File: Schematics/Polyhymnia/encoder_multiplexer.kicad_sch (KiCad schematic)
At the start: 10 parts, among them SW1 Filter Cutoff, SW2 Filter Resonance, SW3 OSC1 Type, SW4 OSC1 Detune, SW5 Filter Resonance, SW6 OSC2 Type, SW7 OSC2 Detune, SW8 OSC3 Type, SW9 OSC3 Detune, U6 ATmega32-16P

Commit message: Cleaned up wiring
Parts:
- removed SW5: Filter Resonance, symbol Device:RotaryEncoder
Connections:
- net 3.3V: now also U6.30 (AVCC)
- net at SW2.A: now also U6.38 (PA2)
- net at SW2.B: now also U6.37 (PA3)
- net at U6.39 (PA1): now also SW1.B
- net at U6.40 (PA0): now also SW1.A

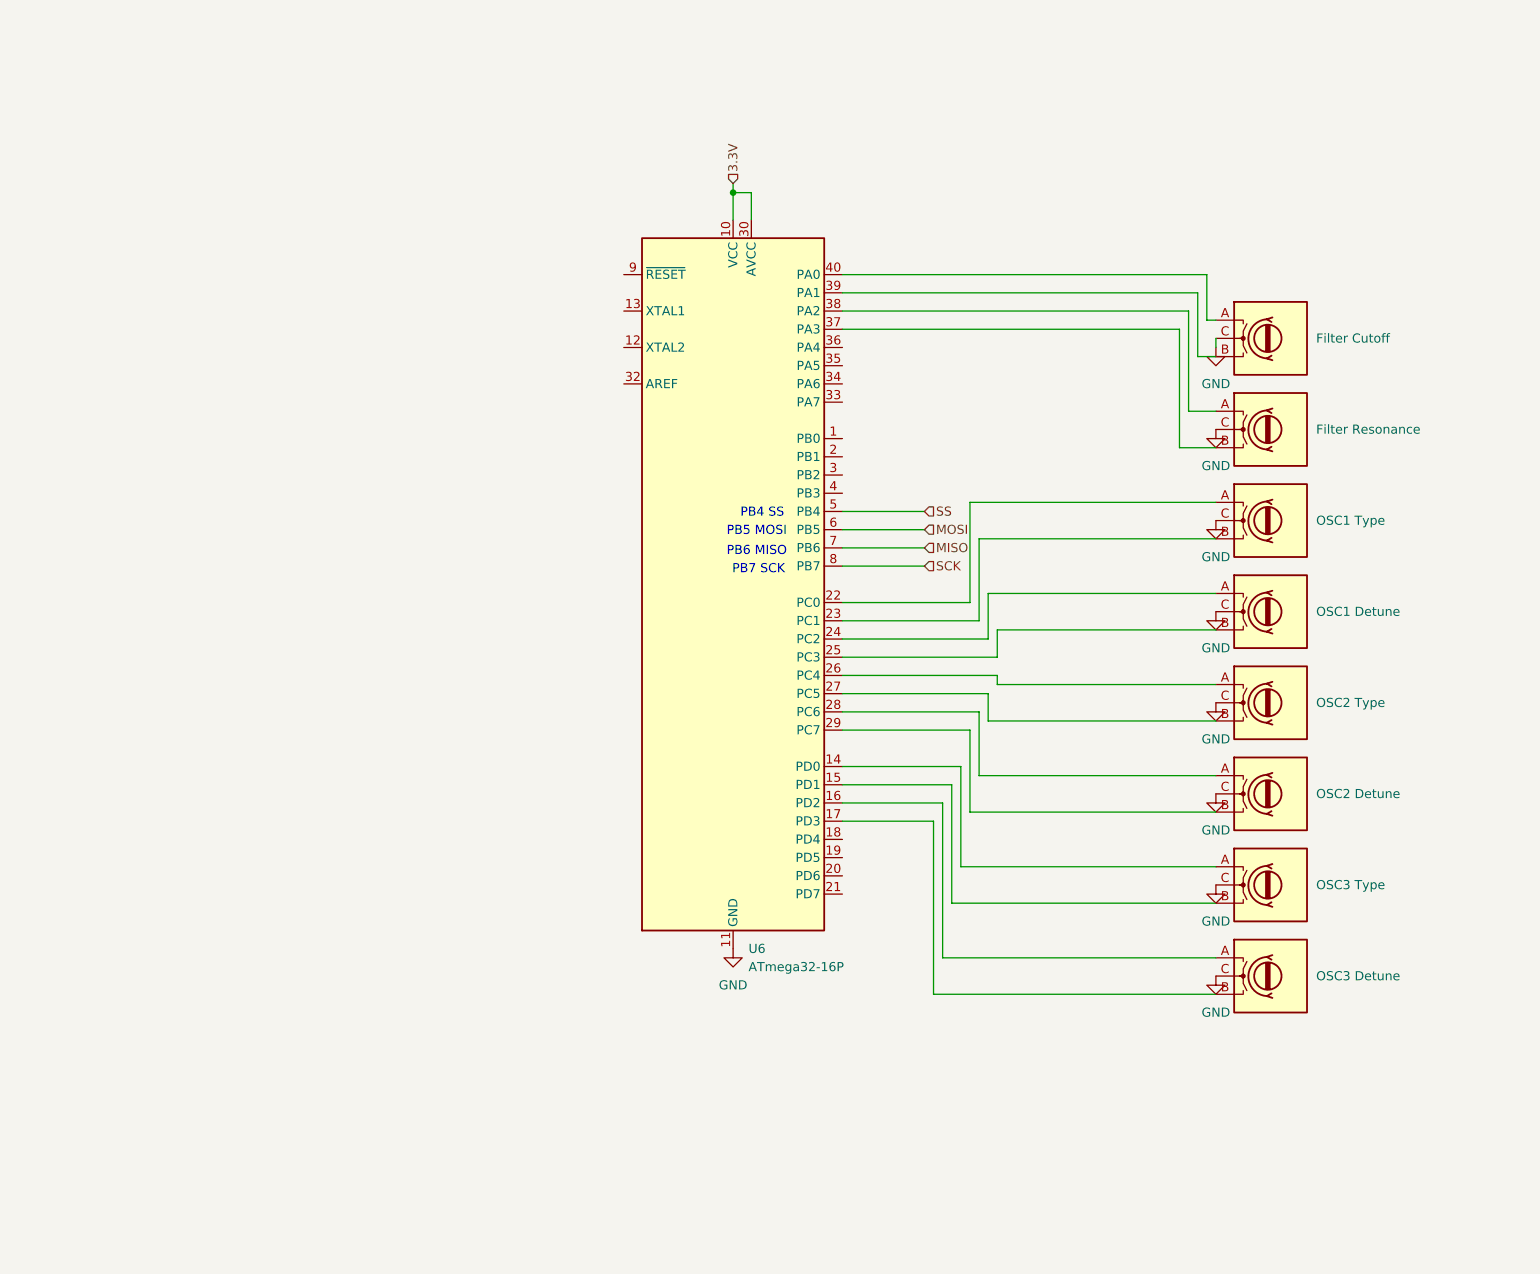
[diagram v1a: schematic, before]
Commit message: Added schematics for OSC, Filter and Envelope and updated README
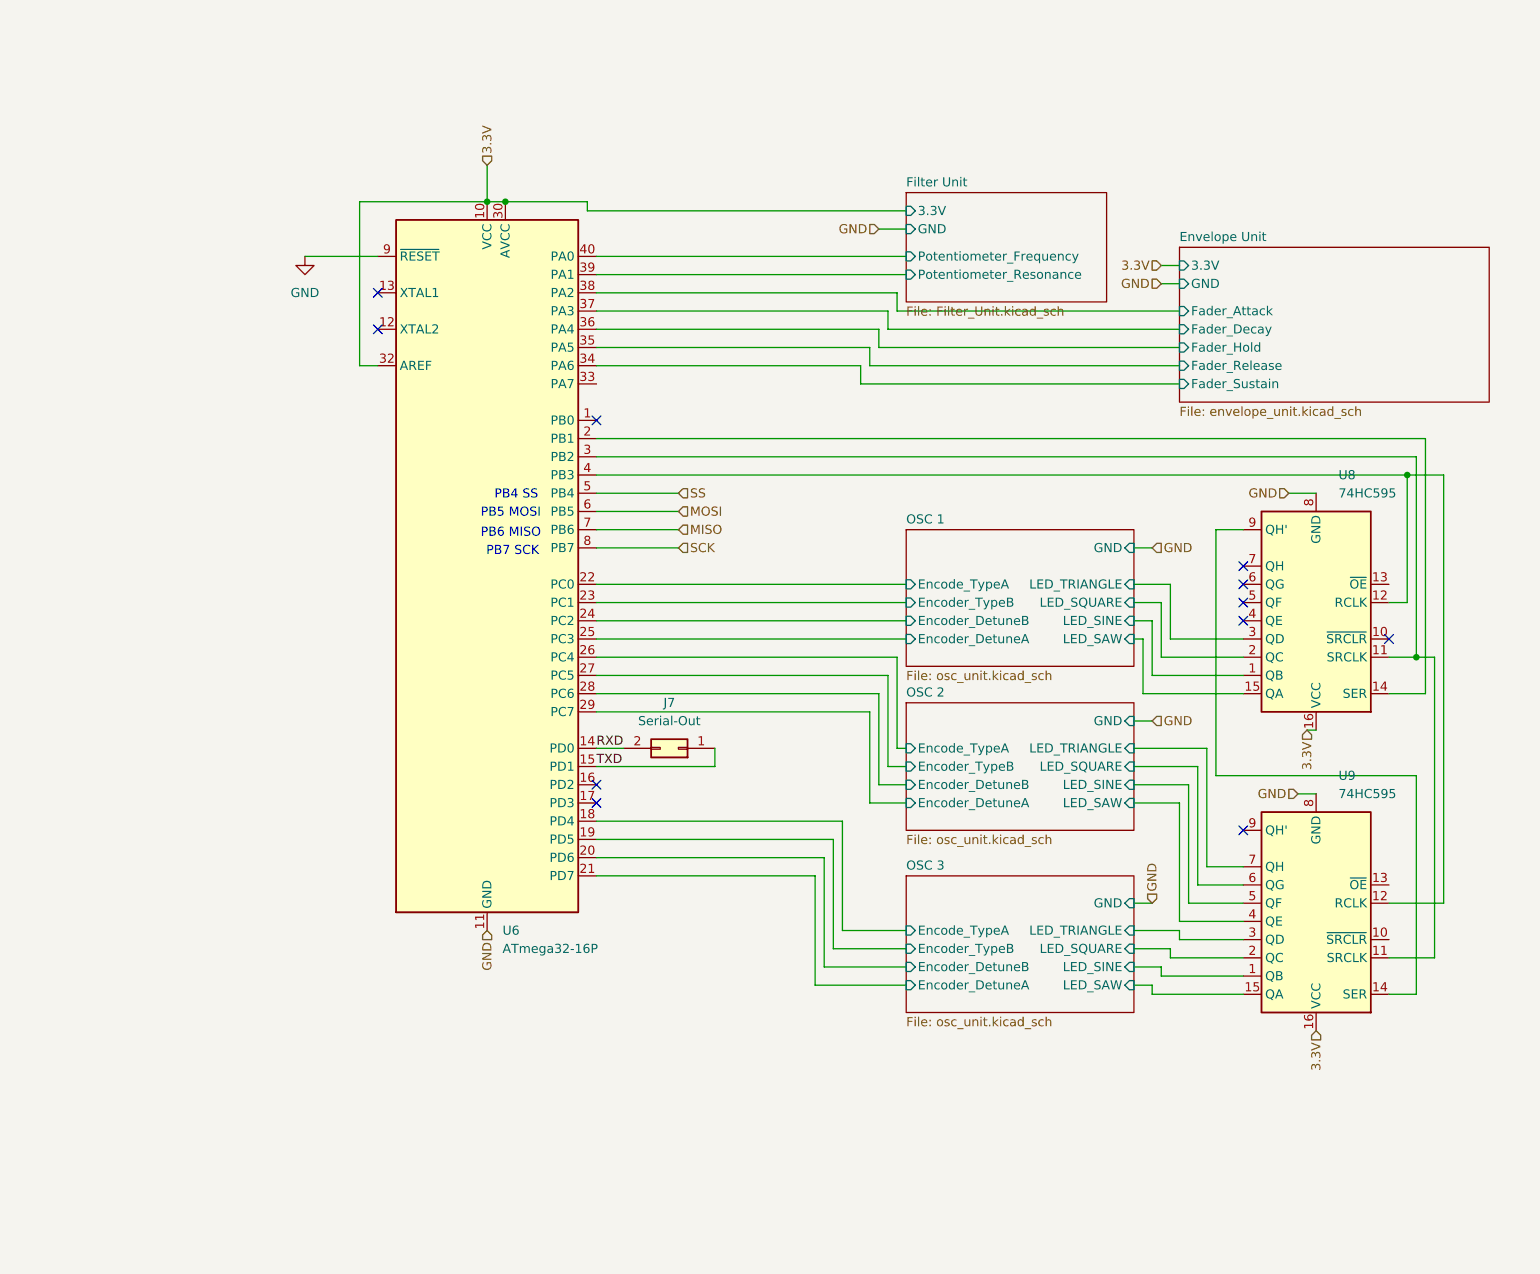
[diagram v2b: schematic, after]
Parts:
- removed SW1: Filter Cutoff, symbol Device:RotaryEncoder
- removed SW2: Filter Resonance, symbol Device:RotaryEncoder
- removed SW3: OSC1 Type, symbol Device:RotaryEncoder
- removed SW4: OSC1 Detune, symbol Device:RotaryEncoder
- removed SW6: OSC2 Type, symbol Device:RotaryEncoder
- removed SW7: OSC2 Detune, symbol Device:RotaryEncoder
- removed SW8: OSC3 Type, symbol Device:RotaryEncoder
- removed SW9: OSC3 Detune, symbol Device:RotaryEncoder
- added J7: Serial-Out, symbol Connector_Generic:Conn_02x01
- added U8, U9: 74HC595, symbol 74xx:74HC595
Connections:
- net 3.3V: now also U6.32 (AREF), U8.16 (VCC), U9.16 (VCC)
- net GND: now also U6.9 (~{RESET}), U8.8 (GND), U9.8 (GND)
- net Envelope Unit/Fader_Attack: now reaches U6.38 (PA2)
- net Envelope Unit/Fader_Decay: now reaches U6.37 (PA3)
- net OSC 2/Encoder_DetuneB: now reaches U6.28 (PC6)
- net OSC 2/Encoder_DetuneA: now reaches U6.29 (PC7)
- net RXD: now reaches U6.14 (PD0)
- net RXD: now also J7.2 (Pin_2)
- net TXD: now reaches U6.15 (PD1)
- net TXD: now also J7.1 (Pin_1)
- net OSC 3/Encode_TypeA: now reaches U6.18 (PD4)
- net OSC 3/Encoder_TypeB: now reaches U6.19 (PD5)
- net at U6.2 (PB1): now also U8.14 (SER)
- net OSC 3/Encoder_DetuneB: now reaches U6.20 (PD6)
- net OSC 3/Encoder_DetuneA: now reaches U6.21 (PD7)
- net OSC 1/Encode_TypeA: now reaches U6.22 (PC0)
- net OSC 1/Encoder_TypeB: now reaches U6.23 (PC1)
- net OSC 1/Encoder_DetuneB: now reaches U6.24 (PC2)
- net OSC 1/Encoder_DetuneA: now reaches U6.25 (PC3)
- net OSC 2/Encode_TypeA: now reaches U6.26 (PC4)
- net OSC 2/Encoder_TypeB: now reaches U6.27 (PC5)
- net at U6.3 (PB2): now also U8.11 (SRCLK), U9.11 (SRCLK)
- net Envelope Unit/Fader_Sustain: now reaches U6.34 (PA6)
- net Envelope Unit/Fader_Release: now reaches U6.35 (PA5)
- net Envelope Unit/Fader_Hold: now reaches U6.36 (PA4)
- net Filter Unit/Potentiometer_Resonance: now reaches U6.39 (PA1)
- net at U6.4 (PB3): now also U8.12 (RCLK), U9.12 (RCLK)
- net Filter Unit/Potentiometer_Frequency: now reaches U6.40 (PA0)
- new net: U8.9 (QH'), U9.14 (SER)
- new net OSC 1/LED_SAW: U8.15 (QA)
- new net OSC 1/LED_SINE: U8.1 (QB)
- new net OSC 1/LED_SQUARE: U8.2 (QC)
- new net OSC 1/LED_TRIANGLE: U8.3 (QD)
- new net OSC 2/LED_SAW: U9.4 (QE)
- new net OSC 2/LED_SINE: U9.5 (QF)
- new net OSC 2/LED_SQUARE: U9.6 (QG)
- new net OSC 2/LED_TRIANGLE: U9.7 (QH)
- new net OSC 3/LED_SAW: U9.15 (QA)
- new net OSC 3/LED_SINE: U9.1 (QB)
- new net OSC 3/LED_SQUARE: U9.2 (QC)
- new net OSC 3/LED_TRIANGLE: U9.3 (QD)
- no-connect marks 0 -> 11
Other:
- added sheet Envelope Unit (envelope_unit.kicad_sch)
- added sheet Filter Unit (Filter_Unit.kicad_sch)
- added sheet OSC 1 (osc_unit.kicad_sch)
- added sheet OSC 2 (osc_unit.kicad_sch)
- added sheet OSC 3 (osc_unit.kicad_sch)
- moved on the sheet: U6

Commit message: Merge
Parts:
- added Q10, Q11, Q12, Q13, Q14, Q15, Q16, Q5, Q6, Q7, Q8, Q9: BC547, PCM_Package_TO_SOT_THT_AKL:TO-92_Inline_Wide_CBE, symbol PCM_Transistor_BJT_AKL:BC547
- added R45, R46, R47, R48, R49, R50, R51, R52, R57, R58, R59, R60: R, symbol Device:R
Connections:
- net 3.3V: now also Q10.1 (C), Q11.1 (C), Q12.1 (C), Q13.1 (C), Q14.1 (C), Q15.1 (C), Q16.1 (C), Q5.1 (C), Q6.1 (C), Q7.1 (C), Q8.1 (C), Q9.1 (C)
- net OSC 1/LED_SAW: now also Q5.3 (E), Q6.3 (E); no longer U8.15 (QA)
- net OSC 1/LED_SQUARE: now also Q7.3 (E); no longer U8.2 (QC)
- net OSC 1/LED_TRIANGLE: now also Q8.3 (E); no longer U8.3 (QD)
- net OSC 2/LED_SAW: now also Q9.3 (E); no longer U9.4 (QE)
- net OSC 2/LED_SINE: now also Q10.3 (E); no longer U9.5 (QF)
- net OSC 2/LED_SQUARE: now also Q12.3 (E); no longer U9.6 (QG)
- net OSC 2/LED_TRIANGLE: now also Q11.3 (E); no longer U9.7 (QH)
- net OSC 3/LED_SAW: now also Q13.3 (E); no longer U9.15 (QA)
- net OSC 3/LED_SINE: now also Q14.3 (E); no longer U9.1 (QB)
- net OSC 3/LED_SQUARE: now also Q16.3 (E); no longer U9.2 (QC)
- net OSC 3/LED_TRIANGLE: now also Q15.3 (E); no longer U9.3 (QD)
- net OSC 1/LED_SINE: no longer names the net of U8.1 (QB)
- net OSC 1/LED_SINE: now also R46.2
- new net: Q10.2 (B), R51.1
- new net: Q12.2 (B), R50.1
- new net: R50.2, U9.6 (QG)
- new net: Q9.2 (B), R52.1
- new net: R52.2, U9.4 (QE)
- new net: Q14.2 (B), R59.1
- new net: Q6.2 (B), R46.1
- new net: R45.2, U8.15 (QA)
- new net: R47.2, U8.2 (QC)
- new net: R48.2, U8.3 (QD)
- new net: Q7.2 (B), R47.1
- new net: Q13.2 (B), R60.1
- new net: Q16.2 (B), R58.1
- new net: Q15.2 (B), R57.1
- new net: R57.2, U9.3 (QD)
- new net: R59.2, U9.1 (QB)
- new net: R60.2, U9.15 (QA)
- new net: R58.2, U9.2 (QC)
- new net: R51.2, U9.5 (QF)
- new net: R49.2, U9.7 (QH)
- new net: Q11.2 (B), R49.1
- new net: Q5.2 (B), R45.1
- new net: Q8.2 (B), R48.1
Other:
- note added: "Basis-Widerstand fehlt noch !!"
- title: (none) -> Encoder Control Unit
- moved on the sheet: J7, U6, U8, U9
